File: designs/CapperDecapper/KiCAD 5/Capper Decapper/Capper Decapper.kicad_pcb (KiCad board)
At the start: 2 copper layers, 94 x 61.6 mm, 48 parts, among them J1 Screw_Terminal_01x02, J2 Conn_01x03_Female, J3 Analog_Zero, J4 Pi_Signals, J5 Motor_Power, K1 AZ850P2-x, U1 L2293, U10 INA214, U11 L2293, U12 INA214, U13 INA214, U2 INA214, U3 INA214, U4 L2293, U5 INA214, U6 INA214, U7 ADP172, U8 L2293, U9 INA214

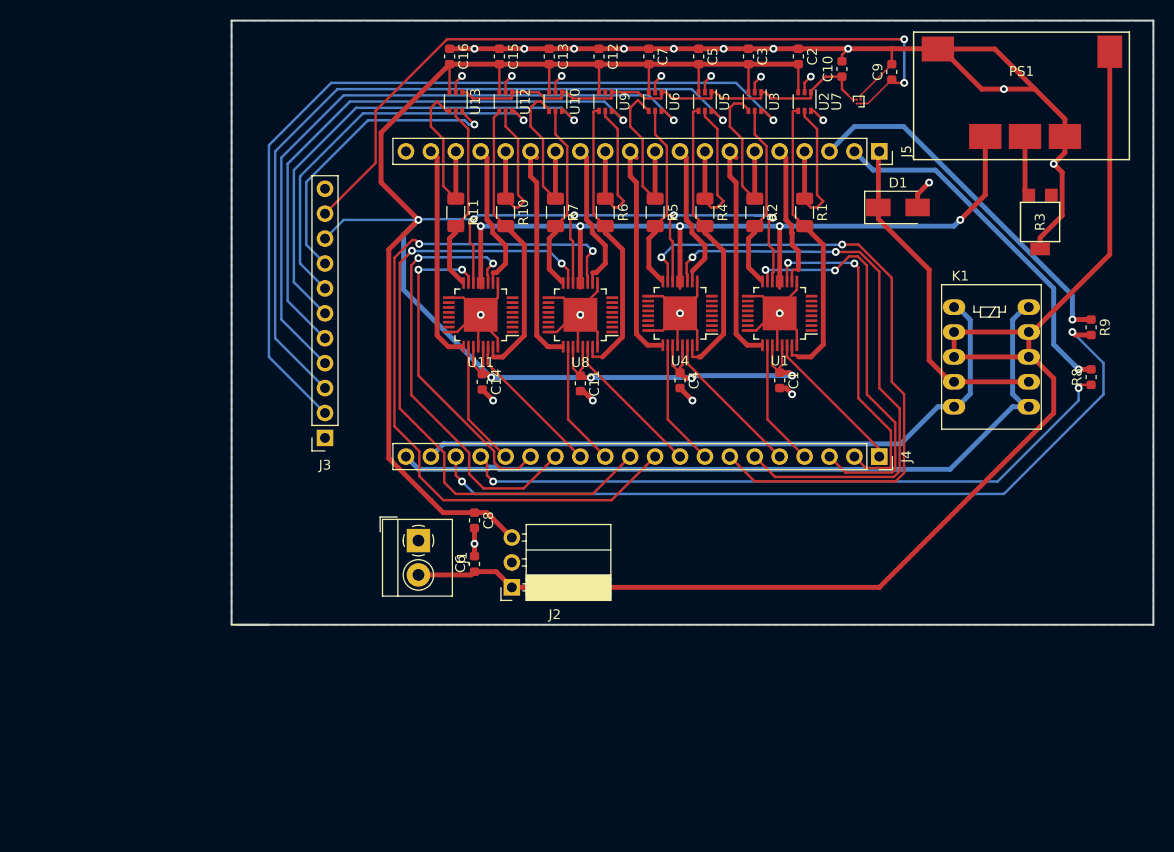
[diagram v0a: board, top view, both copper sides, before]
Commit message: complete 1st draft of capper/decapper PCB
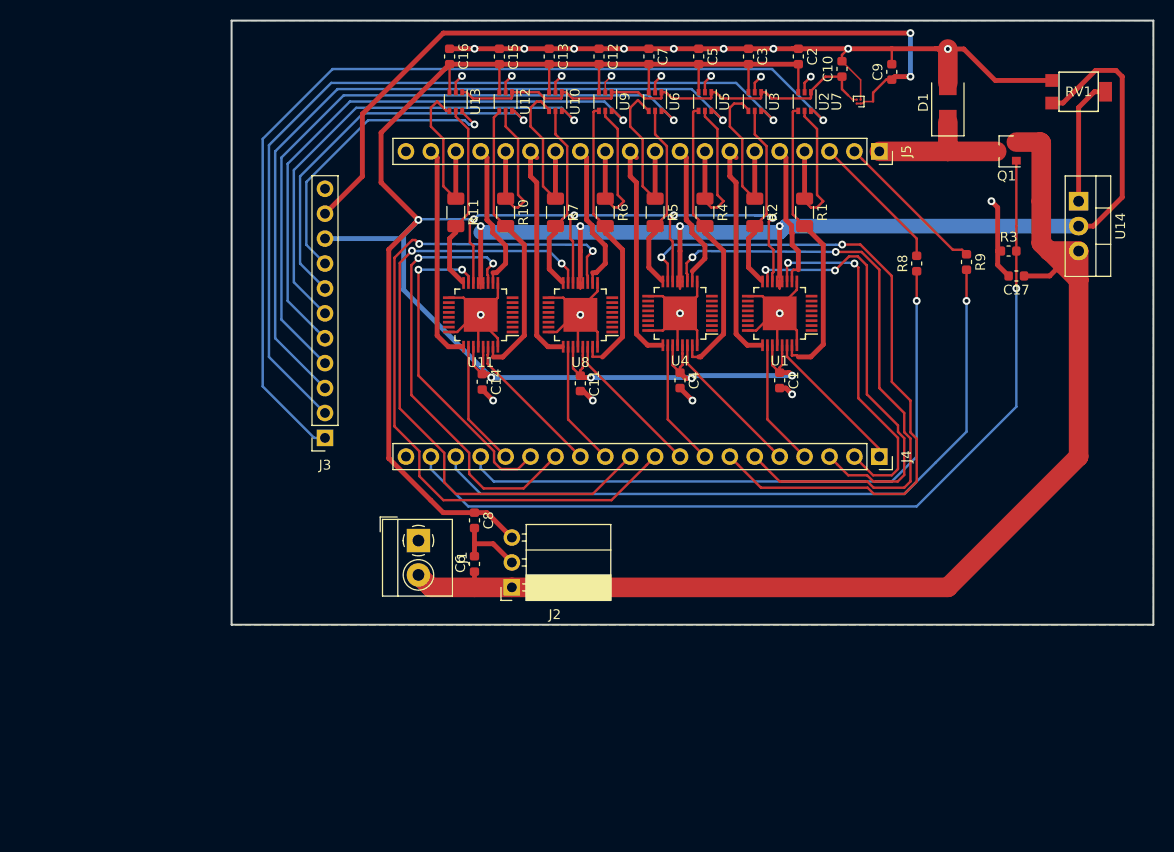
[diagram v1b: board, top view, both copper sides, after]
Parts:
- removed K1: AZ850P2-x, Relay_THT:Relay_DPDT_FRT5
- removed PS1: OKI-T, CustomFootprints:OKI-T
- added C17: C, Capacitor_SMD:C_0603_1608Metric, F.Cu at (179.1, 53.3)
- added Q1: Q_NMOS_GDS, Package_TO_SOT_SMD:SOT-23, F.Cu at (178.1, 40.6)
- added RV1: R_POT, CustomFootprints:R_TRIM_4mm_Gull, F.Cu at (185.4, 35.6)
- added U14: LM338-ADJ, Package_TO_SOT_THT:TO-220-3_Vertical, F.Cu at (185.4, 45.7)
- R3: value RTRIM -> R_US; footprint CustomFootprints:R_TRIM_4mm_Gull -> Resistor_SMD:R_0603_1608Metric
- moved R8 21.2 mm to (168.9, 52.1)
- moved R9 14.3 mm to (174.0, 51.9)
- moved D1 11.8 mm to (172.1, 35.7), turned to 90 degrees
- moved R3 3.70 mm to (178.3, 50.8), turned to 0 degrees
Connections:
- J4 pad 20: /SOLRST -> GND
- R3 pad 1: Net-(PS1-Pad4) -> GND
- R3 pad 2: GND -> /SOLSET
- R8 pad 2: /SW1 -> /SW2
- R9 pad 1: /SW2 -> /SW1
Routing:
- net /ADC1: track 1.65 -> 97.7 mm
- net /SOLRST: track 78.8 -> 0.00 mm
- net /V_motor: track 88.8 -> 120.0 mm, vias 5 -> 4
- net /SOLSET: track 67.4 -> 91.8 mm, vias 0 -> 1
- net /SW2: track 37.3 -> 14.3 mm, vias 1 -> 0
- net /SW1: track 36.7 -> 15.8 mm, vias 1 -> 0
- net /SOL+: track 34.6 -> 15.0 mm
- net GND: track 203.1 -> 189.0 mm, vias 27 -> 26
- net Net-(RV1-Pad2): track 0.00 -> 13.0 mm
- net +36V: track 132.4 -> 121.8 mm
- net Net-(J4-Pad18): track 82.6 -> 73.5 mm, vias 2 -> 1
- net Net-(PS1-Pad4): track 6.12 -> 0.00 mm
- net /MOT4_FWD: track 67.8 -> 71.3 mm
- net /MOT3_REV: track 60.1 -> 63.3 mm
- net Net-(J4-Pad17): track 68.9 -> 66.2 mm, vias 2 -> 1
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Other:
- outline, holes or cut-outs redrawn

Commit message: PWM capper decapper board
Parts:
- removed C16: C, Capacitor_SMD:C_0603_1608Metric
- removed J4: Pi_Signals, Connector_PinSocket_2.54mm:PinSocket_1x20_P2.54mm_Vertical
- removed J5: Motor_Power, Connector_PinSocket_2.54mm:PinSocket_1x20_P2.54mm_Vertical
- removed RV1: R_POT, CustomFootprints:R_TRIM_4mm_Gull
- added C18: 0.01uF, Capacitor_SMD:C_0603_1608Metric, F.Cu at (148.1, 60.3)
- added C19: 0.1uF, Capacitor_SMD:C_0603_1608Metric, F.Cu at (91.1, 56.5)
- added C20: 0.1uF, Capacitor_SMD:C_0603_1608Metric, F.Cu at (145.0, 96.8)
- added C21: 0.1uF, Capacitor_SMD:C_0603_1608Metric, F.Cu at (150.1, 96.7)
- added C22: 22nF, Capacitor_SMD:C_0603_1608Metric, F.Cu at (149.1, 82.1)
- added C23: 22nF, Capacitor_SMD:C_0603_1608Metric, F.Cu at (144.3, 82.1)
- added C24: 0.01uF, Capacitor_SMD:C_0603_1608Metric, F.Cu at (154.9, 96.7)
- added C25: 33uF, Capacitor_SMD:C_0603_1608Metric, F.Cu at (85.9, 89.9)
- added L1: L_Coupled, Inductor_THT:L_CommonMode_Wuerth_WE-CMB-S, F.Cu at (92.5, 83.1)
- added PS1: R-7XX, Resistor_THT:R_Array_SIP12, F.Cu at (108.0, 66.0)
- added R12: 0.05R, Resistor_SMD:R_1206_3216Metric, F.Cu at (134.6, 54.7)
- added R13: 0.05R, Resistor_SMD:R_1206_3216Metric, F.Cu at (139.7, 54.7)
- added R14: 20k, Resistor_SMD:R_0603_1608Metric, F.Cu at (139.2, 86.3)
- added R15: 20k, Resistor_SMD:R_0603_1608Metric, F.Cu at (134.1, 86.4)
- added R16: 0.05R, Resistor_SMD:R_1206_3216Metric, F.Cu at (144.8, 54.7)
- added R17: 0.05R, Resistor_SMD:R_1206_3216Metric, F.Cu at (149.9, 54.7)
- added R18: 20k, Resistor_SMD:R_0603_1608Metric, F.Cu at (149.1, 86.3)
- added R19: 20K, Resistor_SMD:R_0603_1608Metric, F.Cu at (144.3, 86.3)
- C1, C11, C7: value C -> 0.01uF
- C10, C14, C15, C4, C5, C9: value C -> 22nF
- C12, C13, C2, C3, C6, C8: value C -> 0.1uF
- C17: value C -> 33uF
- D1: value D_Schottky_Small_ALT -> Schottky
- J1: value Screw_Terminal_01x02 -> Pi Control Signals; footprint TerminalBlock_4Ucon:TerminalBlock_4Ucon_1x02_P3.50mm_Horizontal -> Connector_PinSocket_2.54mm:PinSocket_1x24_P2.54mm_Vertical
- J2: value Conn_01x03_Female -> Motor_Power; footprint Connector_PinSocket_2.54mm:PinSocket_1x03_P2.54mm_Horizontal -> Connector_PinSocket_2.54mm:PinSocket_1x20_P2.54mm_Vertical
- J3: value Analog_Zero -> Screw_Term; footprint Connector_PinSocket_2.54mm:PinSocket_1x11_P2.54mm_Vertical -> TerminalBlock_4Ucon:TerminalBlock_4Ucon_1x02_P3.50mm_Horizontal
- R1, R2: value R_US -> 330R; footprint Resistor_SMD:R_1206_3216Metric -> Resistor_SMD:R_0603_1608Metric
- R10, R5, R6: value R_US -> 20k; footprint Resistor_SMD:R_1206_3216Metric -> Resistor_SMD:R_0603_1608Metric
- R11: value R_US -> 5k; footprint Resistor_SMD:R_1206_3216Metric -> Resistor_SMD:R_0603_1608Metric
- R3, R8: value R_US -> 0.05R; footprint Resistor_SMD:R_0603_1608Metric -> Resistor_SMD:R_1206_3216Metric
- R4, R7: value R_US -> 0.05R
- R9: value R_US -> 20k
- U10: value INA214 -> L2293; footprint Package_TO_SOT_SMD:SOT-363_SC-70-6 -> Package_QFP:LQFP-32-1EP_5x5mm_P0.5mm_EP3.45x3.45mm
- U11: value L2293 -> V7805-1500R; footprint Package_QFP:LQFP-32-1EP_5x5mm_P0.5mm_EP3.45x3.45mm -> Package_SIP:SIP3_11.6x8.5mm
- U14: value LM338-ADJ -> MAX6018BEUR16; footprint Package_TO_SOT_THT:TO-220-3_Vertical -> Package_TO_SOT_SMD:SOT-23
- U7: value ADP172 -> L2293; footprint Package_BGA:WLP-4_0.86x0.86mm_P0.4mm -> Package_QFP:LQFP-32-1EP_5x5mm_P0.5mm_EP3.45x3.45mm
- U8: value L2293 -> INA214; footprint Package_QFP:LQFP-32-1EP_5x5mm_P0.5mm_EP3.45x3.45mm -> Package_TO_SOT_SMD:SOT-363_SC-70-6
- moved C17 83.7 mm to (103.9, 90.0), turned to 90 degrees
- moved Q1 79.6 mm to (98.7, 46.5), turned to 0 degrees
- moved C2 78.2 mm to (114.6, 96.8), turned to 90 degrees
- moved C3 73.3 mm to (119.6, 96.8), turned to 90 degrees
- moved U2 71.3 mm to (113.7, 91.8), turned to 90 degrees
- moved C7 67.9 mm to (124.7, 96.8), turned to 90 degrees
- moved C13 66.4 mm to (140.0, 96.8), turned to 90 degrees
- moved C12 65.9 mm to (134.9, 96.8), turned to 90 degrees
- moved U3 65.5 mm to (118.7, 91.8), turned to 90 degrees
- moved R3 64.1 mm to (114.3, 54.7), turned to 270 degrees
- moved D1 63.7 mm to (108.7, 41.9), turned to 0 degrees
- moved J1 63.2 mm to (165.7, 38.7), turned to 0 degrees
- moved U13 62.5 mm to (149.2, 91.8), turned to 90 degrees
- moved C10 62.3 mm to (124.0, 82.1)
- moved C9 62.2 mm to (128.8, 82.1), turned to 270 degrees
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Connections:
- C10 pad 1: /V_mon -> /ADC3
- C14 pad 1: /5V -> GND
- C14 pad 2: GND -> /ADC6
- C15 pad 1: GND -> /ADC5
- C15 pad 2: /5V -> GND
- C17 pad 1: +36V -> GND
- C17 pad 2: GND -> Net-(C17-Pad2)
- C4 pad 1: /5V -> GND
- C4 pad 2: GND -> /ADC2
- C5 pad 1: GND -> /ADC1
- C5 pad 2: /5V -> GND
- C6 pad 1: +36V -> /5V
- C8 pad 1: /5V -> GND
- C8 pad 2: GND -> /5V
- C9 pad 1: /3.3V -> GND
- C9 pad 2: GND -> /ADC4
- J1 pad 1: GND -> Net-(J1-Pad1)
- J1 pad 2: +36V -> Net-(J1-Pad2)
- J2 pad 1: +36V -> /SOL+
- J2 pad 2: GND -> /SW1
- J2 pad 3: /5V -> /SW2
- J3 pad 1: /ADC1 -> GND
- J3 pad 2: /ADC2 -> VBUS
- Q1 pad 2: +36V -> VBUS
- R1 pad 1: /MOT1_1 -> Net-(J1-Pad1)
- R1 pad 2: Net-(R1-Pad2) -> /SW2
- R10 pad 1: /MOT7_1 -> /ADC3
- R11 pad 1: /MOT8_1 -> GND
- R11 pad 2: Net-(R11-Pad2) -> /SOLSET
- R2 pad 1: /MOT2_1 -> /SW1
- R2 pad 2: Net-(R2-Pad2) -> Net-(J1-Pad2)
- R3 pad 1: GND -> /MOT1_1
- R3 pad 2: /SOLSET -> Net-(R3-Pad2)
- R4 pad 1: /MOT3_1 -> /MOT2_1
- R5 pad 1: /MOT4_1 -> Net-(R5-Pad1)
- R5 pad 2: Net-(R5-Pad2) -> /ADC2
- R6 pad 1: /MOT5_1 -> /ADC1
- R7 pad 1: /MOT6_1 -> /MOT3_1
- R8 pad 1: Net-(J4-Pad17) -> /MOT4_1
- R8 pad 2: /SW2 -> Net-(R8-Pad2)
- R9 pad 1: /SW1 -> Net-(R9-Pad1)
- R9 pad 2: Net-(J4-Pad18) -> /ADC4
- U1 pad 11: /MOT1_REV -> /REV
- U1 pad 14: /5V -> /EN2
- U1 pad 15: /MOT2_FWD -> /FWD
- U1 pad 16: Net-(R2-Pad2) -> Net-(R4-Pad2)
- U1 pad 26: /MOT2_REV -> /REV
- U1 pad 29: /5V -> /EN1
- U1 pad 30: /MOT1_FWD -> /FWD
- U1 pad 31: Net-(R1-Pad2) -> Net-(R3-Pad2)
- U10 pad 1: /V_mon -> Net-(U10-Pad1)
- U10 pad 2: GND -> Net-(U10-Pad2)
- U10 pad 3: /5V -> Net-(U10-Pad3)
- U10 pad 4: /MOT6_1 -> Net-(U10-Pad4)
- U10 pad 5: Net-(R7-Pad2) -> Net-(U10-Pad5)
- U10 pad 6: /ADC6 -> Net-(U10-Pad6)
- U11 pad 1: Net-(U11-Pad1) -> VBUS
- U11 pad 2: Net-(U11-Pad2) -> GND
- U11 pad 3: Net-(U11-Pad3) -> /5V
- U12 pad 4: Net-(R10-Pad2) -> Net-(R16-Pad2)
- U12 pad 6: /ADC7 -> Net-(R19-Pad2)
- U13 pad 5: Net-(R11-Pad2) -> Net-(R17-Pad2)
- U13 pad 6: /ADC8 -> Net-(R18-Pad1)
- U14 pad 1: Net-(RV1-Pad2) -> /3.3V
- U14 pad 2: /V_motor -> /V_mon
- U14 pad 3: +36V -> GND
- U2 pad 4: Net-(R1-Pad2) -> Net-(R3-Pad2)
- U2 pad 6: /ADC1 -> Net-(R6-Pad2)
- U3 pad 5: Net-(R2-Pad2) -> Net-(R4-Pad2)
- U3 pad 6: /ADC2 -> Net-(R5-Pad1)
- U4 pad 11: /MOT3_REV -> /REV
- U4 pad 14: /5V -> /EN4
- U4 pad 15: /MOT4_FWD -> /FWD
- U4 pad 16: Net-(R5-Pad2) -> Net-(R8-Pad2)
- U4 pad 26: /MOT4_REV -> /REV
- U4 pad 29: /5V -> /EN3
- U4 pad 30: /MOT3_FWD -> /FWD
- U4 pad 31: Net-(R4-Pad2) -> Net-(R7-Pad2)
- U5 pad 4: Net-(R4-Pad2) -> Net-(R7-Pad2)
- U5 pad 6: /ADC3 -> Net-(R10-Pad2)
- U6 pad 5: Net-(R5-Pad2) -> Net-(R8-Pad2)
- U6 pad 6: /ADC4 -> Net-(R9-Pad1)
- U8 pad 1: Net-(U8-Pad1) -> /V_mon
- U8 pad 2: Net-(U8-Pad2) -> GND
- U8 pad 3: Net-(U8-Pad3) -> /5V
- U8 pad 4: Net-(U8-Pad4) -> Net-(R12-Pad2)
- U8 pad 5: Net-(U8-Pad5) -> /MOT5_1
- U9 pad 4: Net-(R6-Pad2) -> /MOT6_1
- U9 pad 5: /MOT5_1 -> Net-(R13-Pad2)
- U9 pad 6: /ADC5 -> Net-(R14-Pad1)
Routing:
- net /REV: track 0.00 -> 143.7 mm, vias 0 -> 8
- net VBUS: track 0.00 -> 127.0 mm
- net /FWD: track 0.00 -> 125.4 mm, vias 0 -> 8
- net +36V: track 121.8 -> 0.00 mm
- net /EN2: track 0.00 -> 81.3 mm, vias 0 -> 2
- net /3.3V: track 82.6 -> 4.89 mm, vias 2 -> 0
- net /MOT5_REV: track 75.3 -> 0.00 mm, vias 2 -> 0
- net Net-(J4-Pad18): track 73.5 -> 0.00 mm, vias 1 -> 0
- net /5V: track 277.5 -> 205.2 mm, vias 9 -> 14
- net /MOT4_FWD: track 71.3 -> 0.00 mm, vias 2 -> 0
- net Net-(J4-Pad17): track 66.2 -> 0.00 mm, vias 1 -> 0
- net /EN1: track 0.00 -> 65.5 mm, vias 0 -> 1
- net /MOT6_FWD: track 65.1 -> 0.00 mm, vias 2 -> 0
- net /EN4: track 0.00 -> 65.1 mm, vias 0 -> 2
- net /MOT3_REV: track 63.3 -> 0.00 mm, vias 2 -> 0
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- added copper zone on In2.Cu, net GND
- removed copper zone on B.Cu, net GND
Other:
- board size 94 x 61.6 mm -> 86.5 x 66.5 mm
- copper layers 2 -> 4
- net class Default: clearance 0.18 -> 0.25
- rule trace_clearance: 0.18 -> 0.25

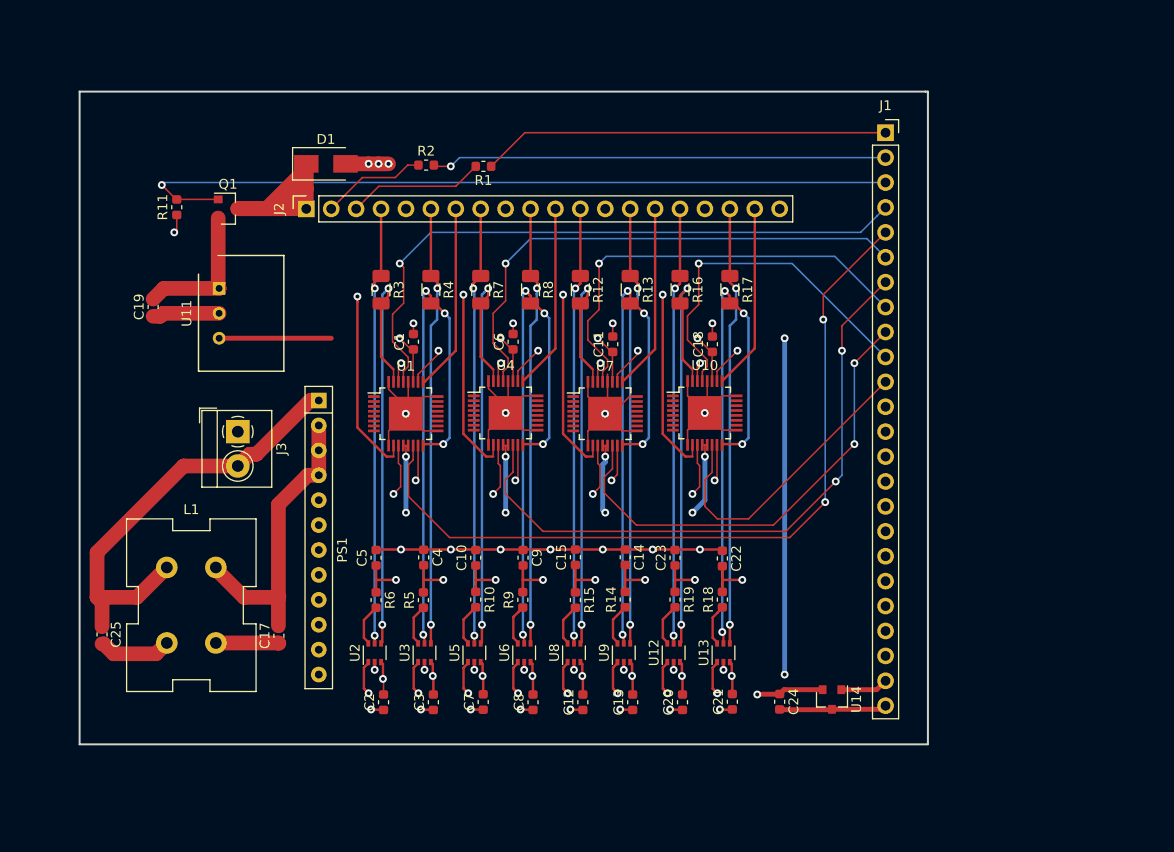
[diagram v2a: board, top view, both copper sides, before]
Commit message: Capper/Decapper HW Control Board Rev A
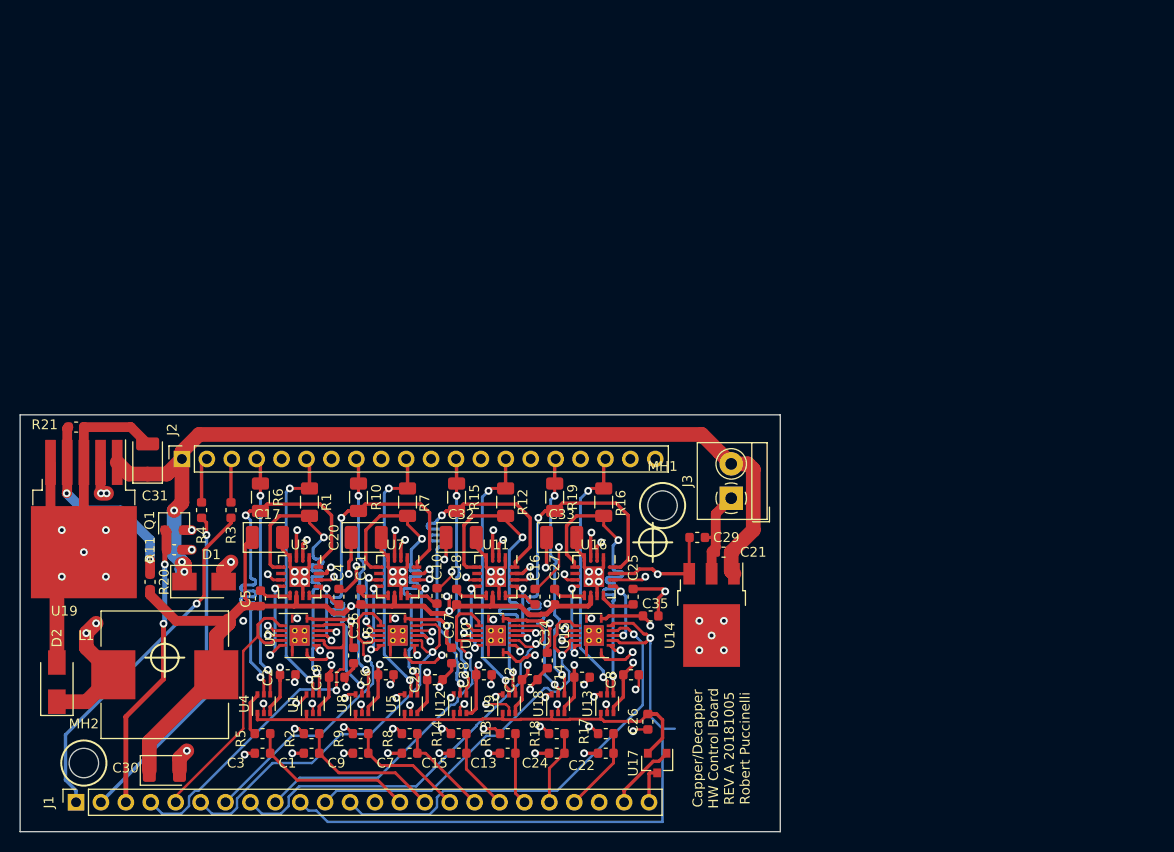
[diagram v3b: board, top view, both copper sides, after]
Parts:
- removed PS1: R-7XX, Resistor_THT:R_Array_SIP12
- added C16: 2.2uF, Capacitor_SMD:C_0603_1608Metric, F.Cu at (130.0, 86.0)
- added C26: 0.01uF, Capacitor_SMD:C_0603_1608Metric, F.Cu at (141.5, 98.8)
- added C27: 10nF, Capacitor_SMD:C_0603_1608Metric, F.Cu at (132.0, 86.0)
- added C28: 0.1uF, Capacitor_SMD:C_0603_1608Metric, F.Cu at (124.8, 94.0)
- added C29: 0.1uF, Capacitor_SMD:C_0603_1608Metric, F.Cu at (146.5, 80.0)
- added C30: 10uF, Capacitor_Tantalum_SMD:CP_EIA-3528-12_Kemet-T, F.Cu at (92.2, 103.8)
- added C31: 10uF, Capacitor_Tantalum_SMD:CP_EIA-3528-12_Kemet-T, F.Cu at (90.5, 72.0)
- added C32: 10uF, Capacitor_Tantalum_SMD:CP_EIA-3528-12_Kemet-T, F.Cu at (122.5, 80.0)
- added C33: 10uF, Capacitor_Tantalum_SMD:CP_EIA-3528-12_Kemet-T, F.Cu at (132.7, 80.0)
- added C34: 0.1uF, Capacitor_SMD:C_0603_1608Metric, F.Cu at (131.2, 92.5)
- added C35: 0.1uF, Capacitor_SMD:C_0603_1608Metric, F.Cu at (141.8, 88.0)
- added C36: 0.1uF, Capacitor_SMD:C_0603_1608Metric, F.Cu at (111.5, 92.0)
- added C37: 0.1uF, Capacitor_SMD:C_0603_1608Metric, F.Cu at (121.5, 92.0)
- added D2: Schottky, Diode_SMD:D_SMA, F.Cu at (81.2, 94.8)
- added MH1: MountingHole, MountingHole:MountingHole_3mm, F.Cu at (143.0, 76.8)
- added MH2: MountingHole, MountingHole:MountingHole_3mm, F.Cu at (84.0, 103.0)
- added R20: 14.2K, Resistor_SMD:R_0603_1608Metric, F.Cu at (90.8, 84.5)
- added R21: 2K, Resistor_SMD:R_0603_1608Metric, F.Cu at (83.2, 68.8)
- added U15: 74AHC08, Package_DFN_QFN:Texas_S-PVQFN-N14_ThermalVias, F.Cu at (136.0, 90.0)
- added U16: DRV8833RTY, Package_DFN_QFN:WQFN-16-1EP_4x4mm_P0.65mm_EP2.1x2.1mm, F.Cu at (136.0, 84.0)
- added U17: MAX6018BEUR16, Package_TO_SOT_SMD:SOT-23, F.Cu at (142.4, 103.0)
- added U18: INA214, Package_TO_SOT_SMD:SOT-363_SC-70-6, F.Cu at (132.3, 97.0)
- added U19: AP1501A, Package_TO_SOT_SMD:TO-263-5_TabPin3, F.Cu at (84.0, 78.1)
- C1, C24, C7: value 0.01uF -> 22nF
- C10, C4: value 22nF -> 2.2uF
- C11, C18: value 0.01uF -> 10nF
- C13, C3: value 0.1uF -> 22nF
- C14, C23: value 22nF -> 0.1uF
- C17: value 33uF -> 10uF; footprint Capacitor_SMD:C_0603_1608Metric -> Capacitor_Tantalum_SMD:CP_EIA-3528-12_Kemet-T
- C20: value 0.1uF -> 10uF; footprint Capacitor_SMD:C_0603_1608Metric -> Capacitor_Tantalum_SMD:CP_EIA-3528-12_Kemet-T
- C21: value 0.1uF -> 0.33uF
- C25: value 33uF -> 2.2uF
- C5: value 22nF -> 10nF
- L1: value L_Coupled -> 22uH; footprint Inductor_THT:L_CommonMode_Wuerth_WE-CMB-S -> Inductor_SMD:L_Wuerth_HCI-1365
- Q1: value Q_NMOS_GDS -> Q_NMOS_GSD
- R1: value 330R -> 0.05R; footprint Resistor_SMD:R_0603_1608Metric -> Resistor_SMD:R_1206_3216Metric
- R10, R15, R6: value 20k -> 0.05R; footprint Resistor_SMD:R_0603_1608Metric -> Resistor_SMD:R_1206_3216Metric
- R13, R17, R8: value 0.05R -> 20k; footprint Resistor_SMD:R_1206_3216Metric -> Resistor_SMD:R_0603_1608Metric
- R19: value 20K -> 0.05R; footprint Resistor_SMD:R_0603_1608Metric -> Resistor_SMD:R_1206_3216Metric
- R2: value 330R -> 20k
- R3, R4: value 0.05R -> 330R; footprint Resistor_SMD:R_1206_3216Metric -> Resistor_SMD:R_0603_1608Metric
- U1, U4: value L2293 -> INA214; footprint Package_QFP:LQFP-32-1EP_5x5mm_P0.5mm_EP3.45x3.45mm -> Package_TO_SOT_SMD:SOT-363_SC-70-6
- U10: value L2293 -> 74AHC08; footprint Package_QFP:LQFP-32-1EP_5x5mm_P0.5mm_EP3.45x3.45mm -> Package_DFN_QFN:Texas_S-PVQFN-N14_ThermalVias
- U11: value V7805-1500R -> DRV8833RTY; footprint Package_SIP:SIP3_11.6x8.5mm -> Package_DFN_QFN:WQFN-16-1EP_4x4mm_P0.65mm_EP2.1x2.1mm
- U14: value MAX6018BEUR16 -> V7805-1500R; footprint Package_TO_SOT_SMD:SOT-23 -> Package_TO_SOT_SMD:TO-252-3_TabPin2
- U2, U6: value INA214 -> 74AHC08; footprint Package_TO_SOT_SMD:SOT-363_SC-70-6 -> Package_DFN_QFN:Texas_S-PVQFN-N14_ThermalVias
- U3: value INA214 -> DRV8833RTY; footprint Package_TO_SOT_SMD:SOT-363_SC-70-6 -> Package_DFN_QFN:WQFN-16-1EP_4x4mm_P0.65mm_EP2.1x2.1mm
- U7: value L2293 -> DRV8833RTY; footprint Package_QFP:LQFP-32-1EP_5x5mm_P0.5mm_EP3.45x3.45mm -> Package_DFN_QFN:WQFN-16-1EP_4x4mm_P0.65mm_EP2.1x2.1mm
- moved J1 107.1 mm to (83.2, 107.0), turned to 90 degrees
- moved R2 59.1 mm to (107.2, 100.0)
- moved C25 54.3 mm to (140.0, 86.0)
- moved J3 50.8 mm to (150.0, 76.0), turned to 90 degrees
- moved R17 47.0 mm to (137.2, 100.0), turned to 0 degrees
- moved R13 47.0 mm to (127.2, 100.0), turned to 0 degrees
- moved R8 46.9 mm to (117.2, 100.0), turned to 0 degrees
- moved D1 44.4 mm to (96.2, 84.5)
- moved C1 43.2 mm to (107.2, 102.0), turned to 0 degrees
- moved C19 42.1 mm to (109.8, 94.2), turned to 0 degrees
- moved U11 40.7 mm to (126.0, 84.0)
- moved R1 38.6 mm to (107.0, 76.4), turned to 90 degrees
- moved U4 38.6 mm to (102.3, 97.0), turned to 90 degrees
- moved C18 36.6 mm to (122.0, 86.0), turned to 270 degrees
- moved C20 36.4 mm to (112.8, 80.0), turned to 0 degrees
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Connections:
- C1 pad 1: /5V -> GND
- C1 pad 2: GND -> /ADC2
- C10 pad 1: /ADC3 -> GND
- C10 pad 2: GND -> Net-(C10-Pad2)
- C11 pad 1: /5V -> Net-(C11-Pad1)
- C11 pad 2: GND -> /V_motor
- C12 pad 1: GND -> /5V
- C12 pad 2: /5V -> GND
- C13 pad 2: /5V -> /ADC6
- C14 pad 1: GND -> /5V
- C14 pad 2: /ADC6 -> GND
- C17 pad 1: GND -> /V_motor
- C17 pad 2: Net-(C17-Pad2) -> GND
- C18 pad 1: /5V -> Net-(C18-Pad1)
- C18 pad 2: GND -> /V_motor
- C19 pad 1: GND -> /5V
- C19 pad 2: VBUS -> GND
- C2 pad 1: GND -> /5V
- C2 pad 2: /5V -> GND
- C20 pad 1: GND -> /V_motor
- C20 pad 2: /5V -> GND
- C21 pad 2: /5V -> VBUS
- C23 pad 1: /ADC7 -> /5V
- C24 pad 1: /V_mon -> /ADC7
- C25 pad 1: VBUS -> GND
- C25 pad 2: GND -> Net-(C25-Pad2)
- C3 pad 1: GND -> /ADC1
- C3 pad 2: /5V -> GND
- C4 pad 2: /ADC2 -> Net-(C4-Pad2)
- C5 pad 1: /ADC1 -> Net-(C5-Pad1)
- C5 pad 2: GND -> /V_motor
- C7 pad 2: /5V -> /ADC4
- C8 pad 1: GND -> /5V
- C8 pad 2: /5V -> GND
- C9 pad 1: GND -> /ADC3
- C9 pad 2: /ADC4 -> GND
- D1 pad 1: /SOL+ -> VBUS
- J1 pad 14: /ADC8 -> /ADC1
- J1 pad 15: /ADC7 -> /ADC2
- J1 pad 16: /ADC6 -> /ADC3
- J1 pad 17: /ADC5 -> /ADC4
- J1 pad 18: /ADC4 -> /ADC5
- J1 pad 19: /ADC3 -> /ADC6
- J1 pad 20: /ADC2 -> /ADC7
- J1 pad 21: /ADC1 -> /ADC8
- J2 pad 1: /SOL+ -> VBUS
- L1 pad 1: VBUS -> Net-(D2-Pad1)
- L1 pad 2: Net-(C17-Pad2) -> /V_motor
- Q1 pad 2: VBUS -> GND
- Q1 pad 3: /SOL+ -> VBUS
- R1 pad 1: Net-(J1-Pad1) -> Net-(R1-Pad1)
- R1 pad 2: /SW2 -> /MOT2_1
- R10 pad 1: /ADC3 -> /MOT3_1
- R12 pad 1: /MOT5_1 -> Net-(R12-Pad1)
- R12 pad 2: Net-(R12-Pad2) -> /MOT6_1
- R13 pad 1: /MOT6_1 -> Net-(R13-Pad1)
- R13 pad 2: Net-(R13-Pad2) -> /ADC6
- R14 pad 1: Net-(R14-Pad1) -> /ADC5
- R14 pad 2: /ADC6 -> Net-(R14-Pad2)
- R15 pad 1: /ADC5 -> /MOT5_1
- R16 pad 1: /MOT7_1 -> Net-(R16-Pad1)
- R16 pad 2: Net-(R16-Pad2) -> /MOT8_1
- R17 pad 1: /MOT8_1 -> Net-(R17-Pad1)
- R17 pad 2: Net-(R17-Pad2) -> /ADC8
- R18 pad 1: Net-(R18-Pad1) -> /ADC7
- R18 pad 2: /ADC8 -> Net-(R18-Pad2)
- R19 pad 1: /ADC7 -> /MOT7_1
- R2 pad 1: /SW1 -> Net-(R2-Pad1)
- R2 pad 2: Net-(J1-Pad2) -> /ADC2
- R3 pad 1: /MOT1_1 -> Net-(J1-Pad1)
- R3 pad 2: Net-(R3-Pad2) -> /SW2
- R4 pad 1: /MOT2_1 -> /SW1
- R4 pad 2: Net-(R4-Pad2) -> Net-(J1-Pad2)
- R5 pad 1: Net-(R5-Pad1) -> /ADC1
- R5 pad 2: /ADC2 -> Net-(R5-Pad2)
- R6 pad 1: /ADC1 -> /MOT1_1
- R7 pad 1: /MOT3_1 -> Net-(R7-Pad1)
- R7 pad 2: Net-(R7-Pad2) -> /MOT4_1
- R8 pad 1: /MOT4_1 -> Net-(R8-Pad1)
- R8 pad 2: Net-(R8-Pad2) -> /ADC4
- R9 pad 1: Net-(R9-Pad1) -> /ADC3
- R9 pad 2: /ADC4 -> Net-(R9-Pad2)
- U1 pad 1: Net-(U1-Pad1) -> /V_mon
- U1 pad 2: Net-(U1-Pad2) -> GND
- U1 pad 3: Net-(U1-Pad3) -> /5V
- U1 pad 4: Net-(U1-Pad4) -> Net-(R1-Pad1)
- U1 pad 5: Net-(U1-Pad5) -> /MOT2_1
- U1 pad 6: Net-(U1-Pad6) -> Net-(R2-Pad1)
- U10 pad 1: Net-(U10-Pad1) -> /FWD
- U10 pad 10: /MOT7_2 -> /EN5
- U10 pad 11: /REV -> Net-(U10-Pad11)
- U10 pad 12: /V_motor -> /REV
- U10 pad 13: /V_motor -> /EN5
- U10 pad 14: /EN8 -> /5V
- U10 pad 15: /FWD -> GND
- U10 pad 2: Net-(U10-Pad2) -> /EN6
- U10 pad 4: Net-(U10-Pad4) -> /REV
- U10 pad 5: Net-(U10-Pad5) -> /EN6
- U10 pad 7: Net-(U10-Pad7) -> GND
- U10 pad 9: GND -> /FWD
- U11 pad 1: VBUS -> GND
- U11 pad 2: GND -> /MOT5_2
- U11 pad 3: /5V -> /MOT6_2
- U12 pad 4: Net-(R16-Pad2) -> /MOT5_1
- U12 pad 5: /MOT7_1 -> Net-(R15-Pad2)
- U12 pad 6: Net-(R19-Pad2) -> Net-(R14-Pad2)
- U13 pad 4: /MOT8_1 -> Net-(R16-Pad1)
- U13 pad 5: Net-(R17-Pad2) -> /MOT8_1
- U13 pad 6: Net-(R18-Pad1) -> Net-(R17-Pad1)
- U14 pad 1: /3.3V -> VBUS
- U14 pad 2: /V_mon -> GND
- U14 pad 3: GND -> /5V
- U2 pad 1: /V_mon -> /FWD
- U2 pad 2: GND -> /EN2
- U2 pad 3: /5V -> Net-(U2-Pad3)
- U2 pad 4: Net-(R3-Pad2) -> /REV
- U2 pad 5: /MOT1_1 -> /EN2
- U2 pad 6: Net-(R6-Pad2) -> Net-(U2-Pad6)
- U3 pad 1: /V_mon -> GND
- U3 pad 2: GND -> /MOT1_2
- U3 pad 3: /5V -> /MOT2_2
- U3 pad 4: /MOT2_1 -> GND
- U3 pad 5: Net-(R4-Pad2) -> Net-(R1-Pad1)
- U3 pad 6: Net-(R5-Pad1) -> Net-(U3-Pad6)
- U4 pad 1: Net-(U4-Pad1) -> /V_mon
- U4 pad 2: Net-(U4-Pad2) -> GND
- U4 pad 3: Net-(U4-Pad3) -> /5V
- U4 pad 4: Net-(U4-Pad4) -> /MOT1_1
- U4 pad 5: Net-(U4-Pad5) -> Net-(R6-Pad2)
- U4 pad 6: Net-(U4-Pad6) -> Net-(R5-Pad2)
- U5 pad 4: Net-(R7-Pad2) -> Net-(R7-Pad1)
- U5 pad 5: /MOT3_1 -> /MOT4_1
- U5 pad 6: Net-(R10-Pad2) -> Net-(R8-Pad1)
- U6 pad 1: /V_mon -> /FWD
- U6 pad 2: GND -> /EN4
- U6 pad 3: /5V -> Net-(U6-Pad3)
- U6 pad 4: /MOT4_1 -> /REV
- U6 pad 5: Net-(R8-Pad2) -> /EN4
- U6 pad 6: Net-(R9-Pad1) -> Net-(U6-Pad6)
- U7 pad 1: Net-(U7-Pad1) -> GND
- U7 pad 10: /MOT5_2 -> /V_motor
- U7 pad 11: /REV -> GND
- U7 pad 12: /V_motor -> Net-(C10-Pad2)
- U7 pad 13: /V_motor -> Net-(U6-Pad11)
- U7 pad 14: /EN6 -> Net-(U6-Pad8)
- U7 pad 15: /FWD -> /5V
- U7 pad 16: Net-(R13-Pad2) -> Net-(R10-Pad2)
- U7 pad 2: Net-(U7-Pad2) -> /MOT3_2
- U7 pad 3: Net-(U7-Pad3) -> /MOT4_2
- U7 pad 4: Net-(U7-Pad4) -> GND
- U7 pad 5: Net-(U7-Pad5) -> Net-(R7-Pad1)
- U7 pad 7: Net-(U7-Pad7) -> Net-(U6-Pad3)
- U7 pad 8: Net-(U7-Pad8) -> Net-(U6-Pad6)
- U7 pad 9: GND -> Net-(C11-Pad1)
- U8 pad 4: Net-(R12-Pad2) -> /MOT3_1
- U8 pad 5: /MOT5_1 -> Net-(R10-Pad2)
- U8 pad 6: Net-(R15-Pad2) -> Net-(R9-Pad2)
- U9 pad 4: /MOT6_1 -> Net-(R12-Pad1)
- U9 pad 5: Net-(R13-Pad2) -> /MOT6_1
- U9 pad 6: Net-(R14-Pad1) -> Net-(R13-Pad1)
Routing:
- net Net-(R4-Pad2): track 55.3 -> 0.00 mm, vias 4 -> 0
- net Net-(R13-Pad2): track 55.3 -> 0.00 mm, vias 4 -> 0
- net Net-(R17-Pad2): track 55.3 -> 0.00 mm, vias 4 -> 0
- net Net-(R8-Pad2): track 55.3 -> 0.00 mm, vias 4 -> 0
- net /EN2: track 81.3 -> 28.8 mm, vias 2 -> 0
- net /SOLSET: track 80.2 -> 29.5 mm, vias 1 -> 2
- net Net-(R12-Pad2): track 46.9 -> 0.00 mm, vias 2 -> 0
- net Net-(R3-Pad2): track 46.9 -> 0.00 mm, vias 2 -> 0
- net Net-(R7-Pad2): track 46.8 -> 0.00 mm, vias 2 -> 0
- net Net-(R16-Pad2): track 46.8 -> 0.00 mm, vias 2 -> 0
- net /ADC1: track 59.5 -> 17.3 mm, vias 1 -> 0
- net /ADC2: track 54.9 -> 14.8 mm, vias 1 -> 0
- net /REV: track 143.7 -> 105.4 mm
- net /ADC3: track 49.8 -> 12.4 mm, vias 1 -> 0
- net Net-(R15-Pad2): track 4.33 -> 40.9 mm, vias 0 -> 2
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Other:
- board size 86.5 x 66.5 mm -> 77.5 x 42.5 mm
- net class Default: clearance 0.25 -> 0.2
- rule pad_to_mask_clearance: 0.2 -> 0
- rule trace_clearance: 0.25 -> 0.2
- rule trace_min: 0.15 -> 0.2
- board text added: "Capper/Decapper HW Control Board REV A 20181005 Robert Puccinelli"
